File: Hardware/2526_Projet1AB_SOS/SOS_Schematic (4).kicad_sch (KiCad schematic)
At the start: 40 parts, among them J4 Conn_ST_STDC14, J5 USB_C_Receptacle_USB2.0_14P, SW1 SW_SPDT, U1 BU33SD5WG-TR, U2 STM32L476RGTx, U3 HTRC11001T, U4 USBLC6-2SC6, Y1 13,56MHz, Y2 8MHz

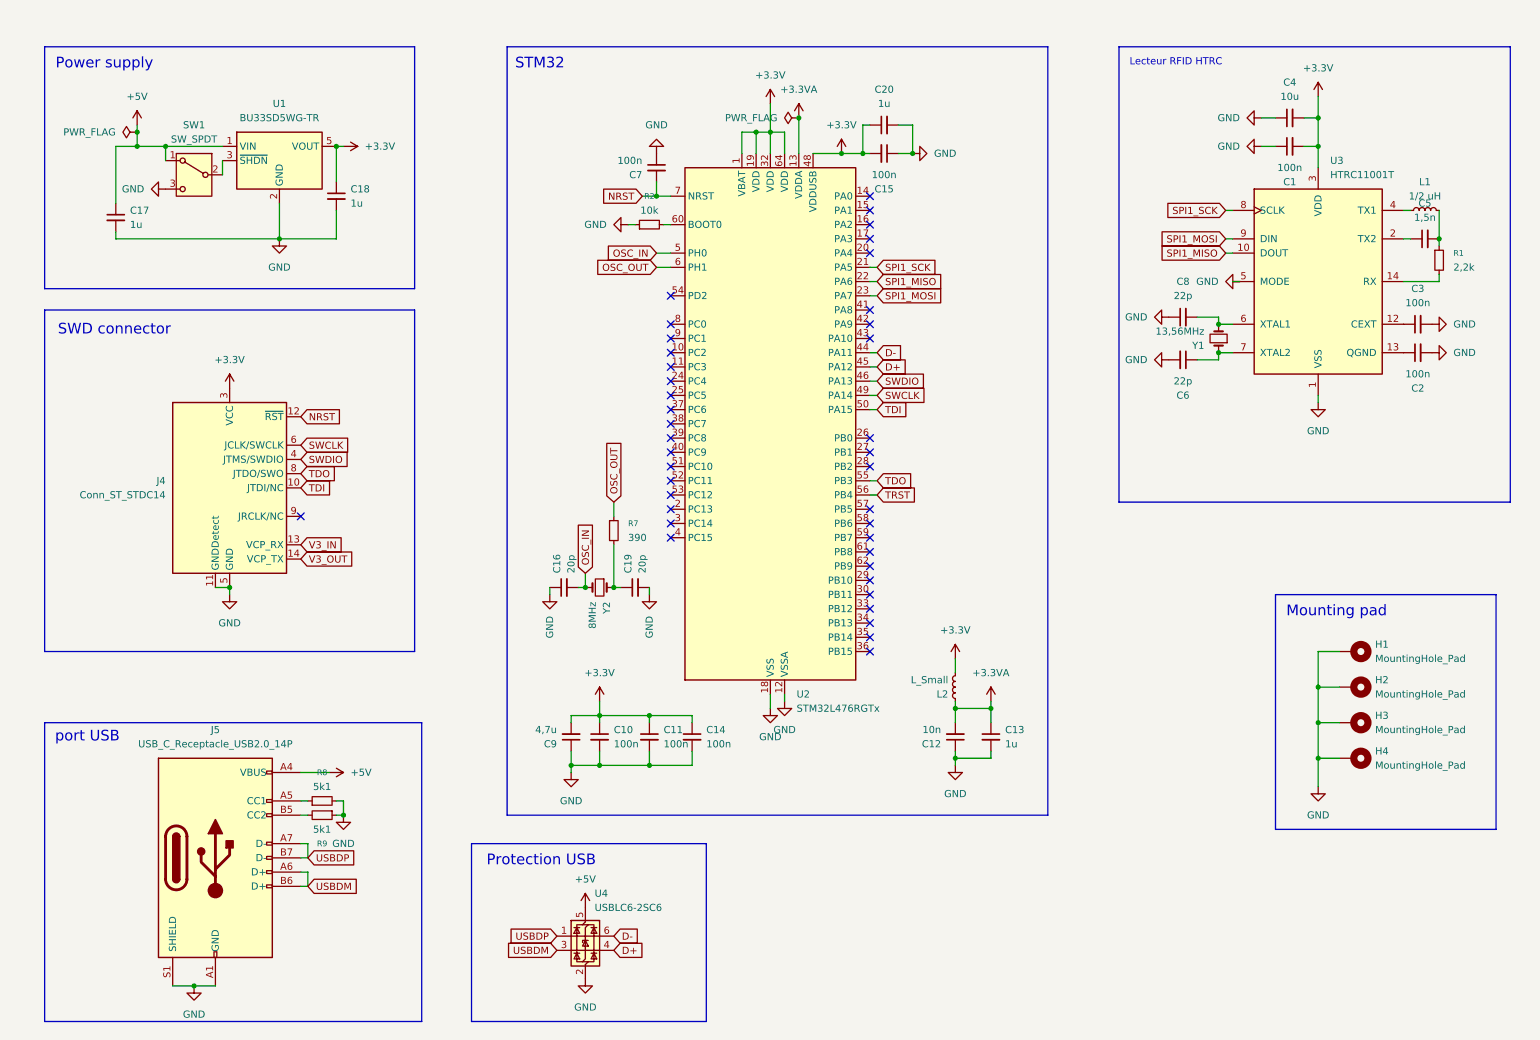
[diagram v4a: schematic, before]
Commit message: update pin list and footprints
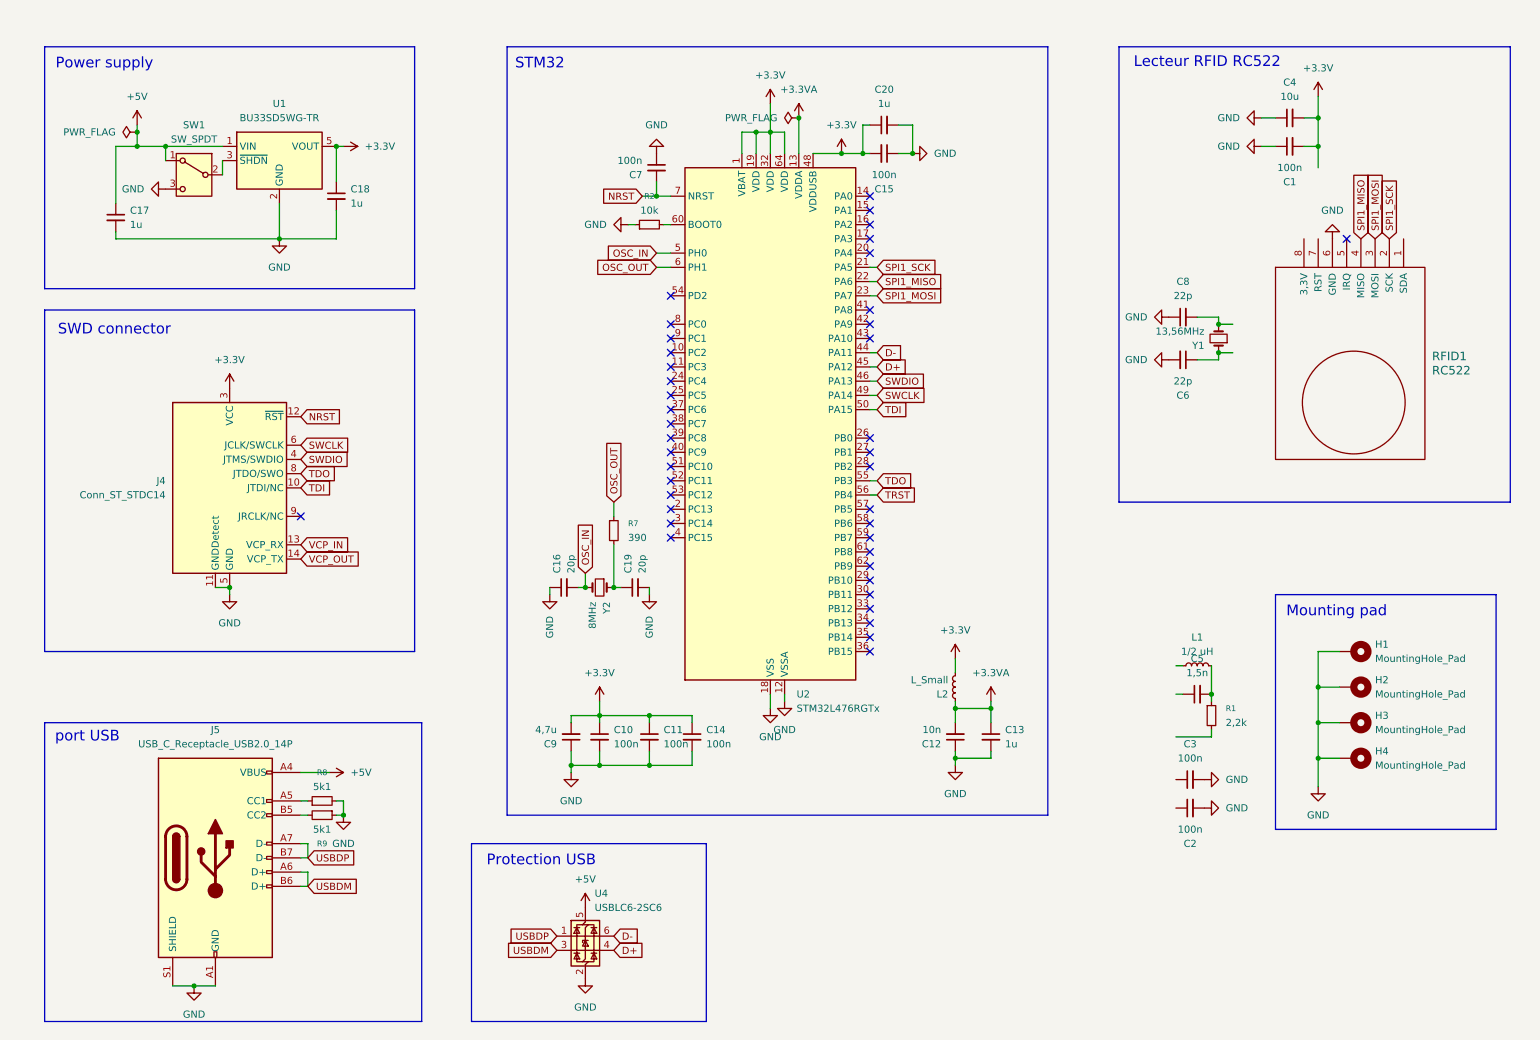
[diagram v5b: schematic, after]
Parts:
- removed U3: HTRC11001T, Package_SO:SOIC-14_3.9x8.7mm_P1.27mm, symbol RF_RFID:HTRC11001T
- added RFID1: RC522, symbol rc522:RC522
- J4: footprint (none) -> Connector:Tag-Connect_TC2070-IDC-FP_2x07_P1.27mm_Vertical
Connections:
- net GND: now also RFID1.6 (GND)
- net SPI1_MISO: now also RFID1.4 (MISO)
- net SPI1_MOSI: now also RFID1.3 (MOSI)
- net SPI1_SCK: now also RFID1.2 (SCK)
- net V3_IN renamed VCP_IN
- net V3_OUT renamed VCP_OUT
- no-connect marks 40 -> 41
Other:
- note added: "Lecteur RFID RC522"
- note removed: "Lecteur RFID HTRC"
- moved on the sheet: C2, C3, C5, L1, R1

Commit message: schematic v2
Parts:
- removed C1, C2, C3, C7: 100n, Capacitor_SMD:C_0603_1608Metric_Pad1.08x0.95mm_HandSolder, symbol Device:C_Small
- removed C12: 10n, Capacitor_SMD:C_0603_1608Metric_Pad1.08x0.95mm_HandSolder, symbol Device:C_Small
- removed C4: 10u, Capacitor_SMD:C_0603_1608Metric_Pad1.08x0.95mm_HandSolder, symbol Device:C_Small
- removed C5: 1,5n, Capacitor_SMD:C_0603_1608Metric_Pad1.08x0.95mm_HandSolder, symbol Device:C_Small
- removed C6, C8: 22p, Capacitor_SMD:C_0603_1608Metric_Pad1.08x0.95mm_HandSolder, symbol Device:C_Small
- removed J5: USB_C_Receptacle_USB2.0_14P, symbol Connector:USB_C_Receptacle_USB2.0_14P
- removed L1: 1/2 uH, Inductor_SMD:L_0805_2012Metric_Pad1.05x1.20mm_HandSolder, symbol Device:L_Small
- removed L2: L_Small, Inductor_SMD:L_0805_2012Metric_Pad1.05x1.20mm_HandSolder, symbol Device:L_Small
- removed R1: 2,2k, Resistor_SMD:R_0805_2012Metric_Pad1.20x1.40mm_HandSolder, symbol Device:R_Small
- removed Y1: 13,56MHz, Crystal:Crystal_DS10_D1.0mm_L4.3mm_Vertical, symbol Device:Crystal_Small
- added C10, C15: 100n, Capacitor_SMD:C_0603_1608Metric, symbol Device:C_Small
- added C14, C16, C17: 10n, Capacitor_SMD:C_0603_1608Metric, symbol Device:C_Small
- added D1, D2, D3: RED, LED_SMD:LED_0603_1608Metric, symbol Device:LED_Small
- added D4: GREEN, LED_SMD:LED_0603_1608Metric, symbol Device:LED_Small
- added D5: BLUE, LED_SMD:LED_0603_1608Metric, symbol Device:LED_Small
- added J1: USB_C_Receptacle_USB2.0_16P, symbol Connector:USB_C_Receptacle_USB2.0_16P
- added R10, R13, R15, R7, R8, R9: 10k, Resistor_SMD:R_0603_1608Metric, symbol Device:R_Small
- added R11, R4: 1k6, Resistor_SMD:R_0603_1608Metric, symbol Device:R_Small
- added R12: 1k1, Resistor_SMD:R_0603_1608Metric, symbol Device:R_Small
- added R14: 670R, Resistor_SMD:R_0603_1608Metric, symbol Device:R_Small
- added R3: 3k3, Resistor_SMD:R_0603_1608Metric, symbol Device:R_Small
- added SW2, SW3, SW4, SW5: SW_Push, Button_Switch_SMD:SW_SPST_B3S-1000, symbol Switch:SW_Push
- added TP4: TP_NSS, TestPoint:TestPoint_Pad_D1.0mm, symbol Connector:TestPoint
- added TP5: TP_SCK, TestPoint:TestPoint_Pad_D1.0mm, symbol Connector:TestPoint
- added TP6: TP_MOSI, TestPoint:TestPoint_Pad_D1.0mm, symbol Connector:TestPoint
- added TP7: TP_MISO, TestPoint:TestPoint_Pad_D1.0mm, symbol Connector:TestPoint
- added TP8: TP_IRQ, TestPoint:TestPoint_Pad_D1.0mm, symbol Connector:TestPoint
- added TP9: TP_RST, TestPoint:TestPoint_Pad_D1.0mm, symbol Connector:TestPoint
- added TP_3V3: TP_3V3, TestPoint:TestPoint_Pad_D1.0mm, symbol Connector:TestPoint
- added TP_5V: TP_5V, TestPoint:TestPoint_Pad_D1.0mm, symbol Connector:TestPoint
- added TP_NRST: TP_NRST, TestPoint:TestPoint_Pad_D1.0mm, symbol Connector:TestPoint
- C1: renamed from C17; footprint Capacitor_SMD:C_0603_1608Metric_Pad1.08x0.95mm_HandSolder -> Capacitor_SMD:C_0603_1608Metric
- C11: renamed from C20; footprint Capacitor_SMD:C_0603_1608Metric_Pad1.08x0.95mm_HandSolder -> Capacitor_SMD:C_0603_1608Metric
- C12: renamed from C15; footprint Capacitor_SMD:C_0603_1608Metric_Pad1.08x0.95mm_HandSolder -> Capacitor_SMD:C_0603_1608Metric
- C13: footprint Capacitor_SMD:C_0603_1608Metric_Pad1.08x0.95mm_HandSolder -> Capacitor_SMD:C_0603_1608Metric
- C2: renamed from C18; footprint Capacitor_SMD:C_0603_1608Metric_Pad1.08x0.95mm_HandSolder -> Capacitor_SMD:C_0603_1608Metric
- C3: renamed from C9; value 4,7u -> 4u7; footprint Capacitor_SMD:C_0603_1608Metric_Pad1.08x0.95mm_HandSolder -> Capacitor_SMD:C_0603_1608Metric
- C4: renamed from C16; footprint Capacitor_SMD:C_0603_1608Metric_Pad1.08x0.95mm_HandSolder -> Capacitor_SMD:C_0603_1608Metric
- C5: renamed from C10; footprint Capacitor_SMD:C_0603_1608Metric_Pad1.08x0.95mm_HandSolder -> Capacitor_SMD:C_0603_1608Metric
- C6: renamed from C11; footprint Capacitor_SMD:C_0603_1608Metric_Pad1.08x0.95mm_HandSolder -> Capacitor_SMD:C_0603_1608Metric
- C7: renamed from C19; footprint Capacitor_SMD:C_0603_1608Metric_Pad1.08x0.95mm_HandSolder -> Capacitor_SMD:C_0603_1608Metric
- C9: renamed from C14; footprint Capacitor_SMD:C_0603_1608Metric_Pad1.08x0.95mm_HandSolder -> Capacitor_SMD:C_0603_1608Metric
- H1, H2, H3, H4: footprint MountingHole:MountingHole_3.2mm_M3_DIN965_Pad -> MountingHole:MountingHole_3.2mm_M3_Pad
- J2: renamed from J4; footprint Connector:Tag-Connect_TC2070-IDC-FP_2x07_P1.27mm_Vertical -> Connector_PinHeader_1.27mm:PinHeader_2x07_P1.27mm_Vertical_SMD
- R1: renamed from R8; footprint Resistor_SMD:R_0805_2012Metric_Pad1.20x1.40mm_HandSolder -> Resistor_SMD:R_0603_1608Metric
- R2: renamed from R9; footprint Resistor_SMD:R_0805_2012Metric_Pad1.20x1.40mm_HandSolder -> Resistor_SMD:R_0603_1608Metric
- R5: renamed from R7; footprint Resistor_SMD:R_0805_2012Metric_Pad1.20x1.40mm_HandSolder -> Resistor_SMD:R_0603_1608Metric
- R6: renamed from R2; footprint Resistor_SMD:R_0805_2012Metric_Pad1.20x1.40mm_HandSolder -> Resistor_SMD:R_0603_1608Metric
- RFID1: footprint (none) -> Connector_PinSocket_2.54mm:PinSocket_1x08_P2.54mm_Vertical
- Y1: renamed from Y2; value 8MHz -> 20MHz; footprint Crystal:Crystal_DS10_D1.0mm_L4.3mm_Vertical -> Crystal:Crystal_SMD_HC49-SD; MPN (none) -> ABLS-16.000MHZ-20-B-3-H-T
- renumbered U4 to U2, U2 to U3
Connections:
- net +3.3VA is gone; now on net +3.3V: C13.1, U3.13 (VDDA)
- net VCP_IN is gone; now on net UART_RX: J2.13 (VCP_RX)
- net VCP_OUT is gone; now on net UART_TX: J2.14 (VCP_TX)
- net +3.3V: now also RFID1.8 (3,3V), C10.1, R4.1, SW2.1, SW4.1, SW5.1, TP_3V3.1
- net +5V: now also J1.A4 (VBUS), J1.A9 (VBUS), J1.B4 (VBUS), J1.B9 (VBUS), R3.1, TP_5V.1
- net GND: now also C10.2, C14.2, C15.2, C16.2, C17.2, D1.1 (K), D2.1 (K), D3.1 (K), D4.1 (K), D5.1 (K), J1.A1 (GND), J1.A12 (GND), J1.B1 (GND), J1.B12 (GND), J1.S1 (SHIELD), R10.2, R15.2, R8.2, SW3.2
- net NRST: now also C15.1, SW3.1, TP_NRST.1
- net SPI1_MISO: now also TP7.1
- net SPI1_MOSI: now also TP6.1
- net SPI1_SCK: now also TP5.1
- net USBDM: now also J1.A6 (D+), J1.B6 (D+)
- net USBDP: now also J1.A7 (D-), J1.B7 (D-)
- net SPI1_CS: now reaches RFID1.1 (SDA)
- net SPI1_CS: now also U3.20 (PA4), TP4.1
- net RC522_IRQ: now reaches RFID1.5 (IRQ)
- net RC522_IRQ: now also U3.25 (PC5), TP8.1
- net RC522_RST: now reaches RFID1.7 (RST)
- net RC522_RST: now also U3.24 (PC4), TP9.1
- net USR_LED_1: now reaches U3.33 (PB12)
- net USR_LED_1: now also R11.1
- net USR_LED_2: now reaches U3.34 (PB13)
- net USR_LED_2: now also R12.1
- net USR_LED_3: now reaches U3.35 (PB14)
- net USR_LED_3: now also R14.1
- net USR_BTN_1: now reaches U3.37 (PC6)
- net USR_BTN_1: now also C14.1, R7.1
- net USR_BTN_2: now reaches U3.38 (PC7)
- net USR_BTN_2: now also C16.1, R9.1
- net USR_BTN_3: now reaches U3.39 (PC8)
- net USR_BTN_3: now also C17.1, R13.1
- net UART_TX: now reaches U3.51 (PC10)
- net UART_RX: now reaches U3.52 (PC11)
- net at R2.2: now also J1.B5 (CC2)
- net at R1.1: now also J1.A5 (CC1)
- net TDI: no longer names the net of J2.10 (JTDI/NC)
- net TDI: no longer U3.50 (PA15)
- net TDO renamed SWO
- net TRST: no longer names the net of U3.56 (PB4)
- new net: R7.2, R8.1, SW2.2
- new net: D4.2 (A), R12.2
- new net: R13.2, R15.1, SW5.2
- new net: D3.2 (A), R11.2
- new net: R10.1, R9.2, SW4.2
- new net: D1.2 (A), R3.2
- new net: D5.2 (A), R14.2
- new net: D2.2 (A), R4.2
- no-connect marks 41 -> 34
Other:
- note added: "1.7V @ 1mA"
- note added: "2.2V @ 1mA"
- note added: "2.6V @ 1mA"
- moved on the sheet: C1, C11, C12, C2, C3, C4, C5, C6, C7, C9, H1, H2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

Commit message: BOM
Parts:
- TP_3V3: value TP_3V3 -> TestPoint
- TP_5V1: renamed from TP_5V; value TP_5V -> TestPoint
- TP_IRQ1: renamed from TP8; value TP_IRQ -> TestPoint
- TP_MISO1: renamed from TP7; value TP_MISO -> TestPoint
- TP_MOSI1: renamed from TP6; value TP_MOSI -> TestPoint
- TP_NRST1: renamed from TP_NRST; value TP_NRST -> TestPoint
- TP_NSS1: renamed from TP4; value TP_NSS -> TestPoint
- TP_RST1: renamed from TP9; value TP_RST -> TestPoint
- TP_SCK1: renamed from TP5; value TP_SCK -> TestPoint
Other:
- note added: "Buttons&LEDs"
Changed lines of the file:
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@@
 	)
 	(rectangle
+		(start 180.34 60.96)
+		(end 283.21 130.81)
+		(stroke
+			(width 0)
+			(type default)
+		)
+		(fill
+			(type none)
+		)
+	)
+	(rectangle
 		(start 13.97 124.46)
 		(end 80.01 194.31)
@@
 		)
 	)
+	(text "Buttons&LEDs"
+		(exclude_from_sim no)
+		(at 191.516 64.262 0)
+		(effects
+			(font
+				(size 1.905 1.905)
+			)
+		)
+	)
 	(text "1.7V @ 1mA"
 		(exclude_from_sim no)
@@
 		(on_board yes)
 		(dnp no)
-		(property "Reference" "TP8"
+		(property "Reference" "TP_IRQ1"
 			(at 232.156 22.86 0)
 			(effects
@@
 			)
 		)
-		(property "Value" "TP_IRQ"
+		(property "Value" "TestPoint"
 			(at 232.41 32.766 90)
 			(effects
@@
 				)
 				(justify left)
+				(hide yes)
 			)
 		)
@@
 			(project "SOS_Schematic (4)"
 				(path "/9d394b3d-e5c0-4919-a596-896a666dc5cf"
-					(reference "TP8")
+					(reference "TP_IRQ1")
 					(unit 1)
 				)
@@
 		(on_board yes)
 		(dnp no)
-		(property "Reference" "TP9"
+		(property "Reference" "TP_RST1"
 			(at 237.236 22.86 0)
 			(effects
@@
 			)
 		)
-		(property "Value" "TP_RST"
+		(property "Value" "TestPoint"
 			(at 237.49 33.02 90)
 			(effects
@@
 				)
 				(justify left)
+				(hide yes)
 			)
 		)
@@
 			(project "SOS_Schematic (4)"
 				(path "/9d394b3d-e5c0-4919-a596-896a666dc5cf"
-					(reference "TP9")
+					(reference "TP_RST1")
 					(unit 1)
 				)
@@
 		(on_board yes)
 		(dnp no)
-		(property "Reference" "TP6"
+		(property "Reference" "TP_MOSI1"
 			(at 221.996 22.86 0)
 			(effects
@@
 			)
 		)
-		(property "Value" "TP_MOSI"
+		(property "Value" "TestPoint"
 			(at 222.504 33.274 90)
 			(effects
@@
 				)
 				(justify left)
+				(hide yes)
 			)
 		)
@@
 			(project "SOS_Schematic (4)"
 				(path "/9d394b3d-e5c0-4919-a596-896a666dc5cf"
-					(reference "TP6")
+					(reference "TP_MOSI1")
 					(unit 1)
 				)
@@
 			)
 		)
-		(property "Value" "TP_3V3"
+		(property "Value" "TestPoint"
 			(at 59.69 27.1779 0)
 			(effects
@@
 		(on_board yes)
 		(dnp no)
-		(property "Reference" "TP5"
+		(property "Reference" "TP_SCK1"
 			(at 216.916 22.86 0)
 			(effects
@@
 			)
 		)
-		(property "Value" "TP_SCK"
+		(property "Value" "TestPoint"
 			(at 217.17 32.512 90)
 			(effects
@@
 				)
 				(justify left)
+				(hide yes)
 			)
 		)
@@
 			(project "SOS_Schematic (4)"
 				(path "/9d394b3d-e5c0-4919-a596-896a666dc5cf"
-					(reference "TP5")
+					(reference "TP_SCK1")
 					(unit 1)
 				)
@@
 		(dnp no)
 		(fields_autoplaced yes)
-		(property "Reference" "TP_NRST"
+		(property "Reference" "TP_NRST1"
 			(at 64.77 75.4379 0)
 			(effects
@@
 			)
 		)
-		(property "Value" "TP_NRST"
+		(property "Value" "TestPoint"
 			(at 64.77 77.9779 0)
 			(effects
@@
 			(project "SOS_Schematic (4)"
 				(path "/9d394b3d-e5c0-4919-a596-896a666dc5cf"
-					(reference "TP_NRST")
+					(reference "TP_NRST1")
 					(unit 1)
 				)
@@
 		(on_board yes)
 		(dnp no)
-		(property "Reference" "TP4"
+		(property "Reference" "TP_NSS1"
 			(at 211.836 22.86 0)
 			(effects
@@
 			)
 		)
-		(property "Value" "TP_NSS"
+		(property "Value" "TestPoint"
 			(at 212.09 31.75 90)
 			(effects
@@
 				)
 				(justify left)
+				(hide yes)
 			)
 		)
@@
 			(project "SOS_Schematic (4)"
 				(path "/9d394b3d-e5c0-4919-a596-896a666dc5cf"
-					(reference "TP4")
+					(reference "TP_NSS1")
 					(unit 1)
 				)
@@
 		(on_board yes)
 		(dnp no)
-		(property "Reference" "TP7"
+		(property "Reference" "TP_MISO1"
 			(at 227.076 22.86 0)
 			(effects
@@
 			)
 		)
-		(property "Value" "TP_MISO"
+		(property "Value" "TestPoint"
 			(at 227.584 33.782 90)
 			(effects
@@
 				)
 				(justify left)
+				(hide yes)
 			)
 		)
@@
 			(project "SOS_Schematic (4)"
 				(path "/9d394b3d-e5c0-4919-a596-896a666dc5cf"
-					(reference "TP7")
+					(reference "TP_MISO1")
 					(unit 1)
 				)
@@
 		(dnp no)
 		(fields_autoplaced yes)
-		(property "Reference" "TP_5V"
+		(property "Reference" "TP_5V1"
 			(at 17.018 24.13 90)
 			(effects
@@
 			)
 		)
-		(property "Value" "TP_5V"
+		(property "Value" "TestPoint"
 			(at 17.018 26.67 90)
 			(effects
@@
 			(project ""
 				(path "/9d394b3d-e5c0-4919-a596-896a666dc5cf"
-					(reference "TP_5V")
+					(reference "TP_5V1")
 					(unit 1)
 				)
